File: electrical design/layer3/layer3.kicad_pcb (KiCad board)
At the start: 2 copper layers, 150 x 137.9 mm, 42 parts, among them J1 SH1.0 5P, J10 SH1.0 2P, J11 LAYER1, J12 XH2.54 2P, J2 SH1.0 5P, J3 SH1.0 5P, J4 SH1.0 5P, J5 XH2.54 5P, J6 CAMERA1, J7 CAMERA2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

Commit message: resolve some l2 and l3 board issues
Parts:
- removed R8: 10k, Resistor_SMD:R_0603_1608Metric
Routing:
- net +3V3: track 300.0 -> 295.4 mm
- net /M4CS: track 81.1 -> 84.4 mm
- net /STRAT4: track 48.2 -> 44.9 mm
- net /EN: track 117.9 -> 115.6 mm
- net /STRAT3: track 40.1 -> 39.1 mm
- net +5V: track 363.7 -> 362.8 mm
- net /M3INA: track 60.5 -> 59.8 mm
- net /STRAT2: track 31.0 -> 31.8 mm
- net /M4INA: track 87.8 -> 87.0 mm
- net GNDD: vias 79 -> 126

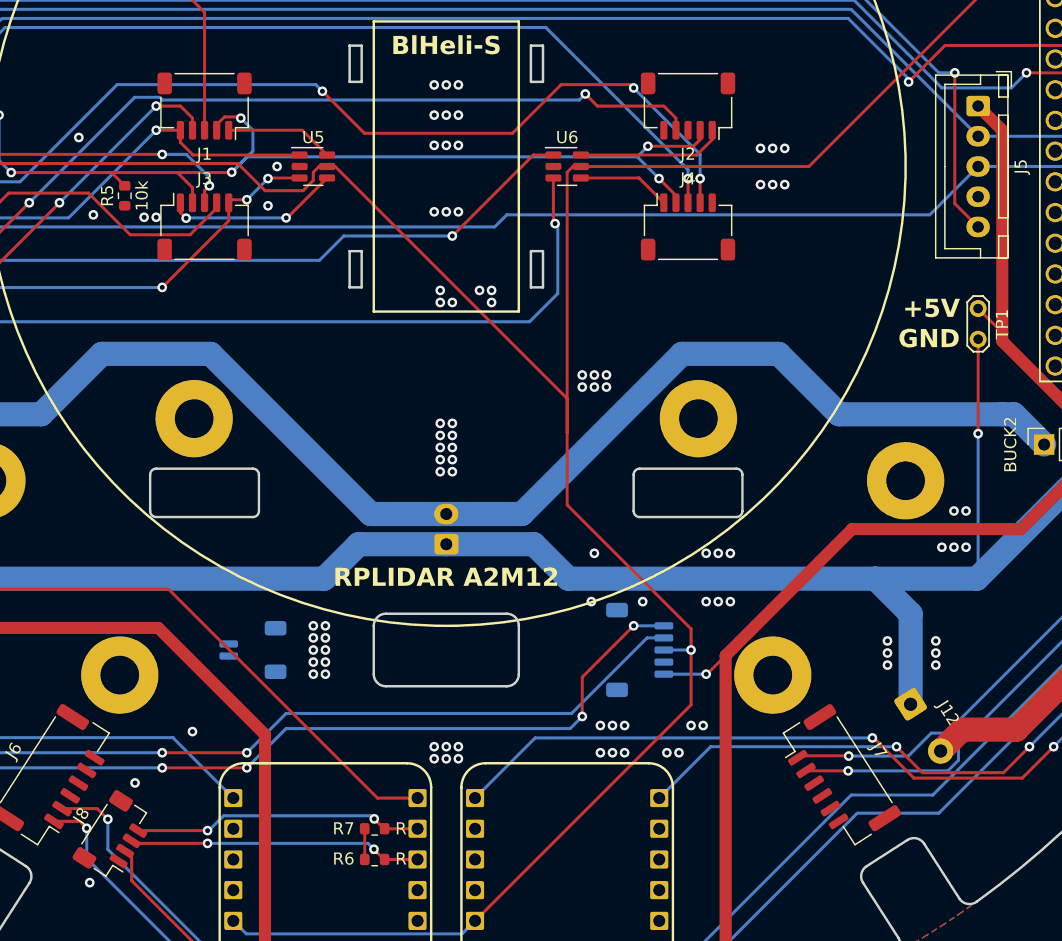
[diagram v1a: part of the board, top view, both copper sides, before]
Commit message: add jlc order number silkscreen
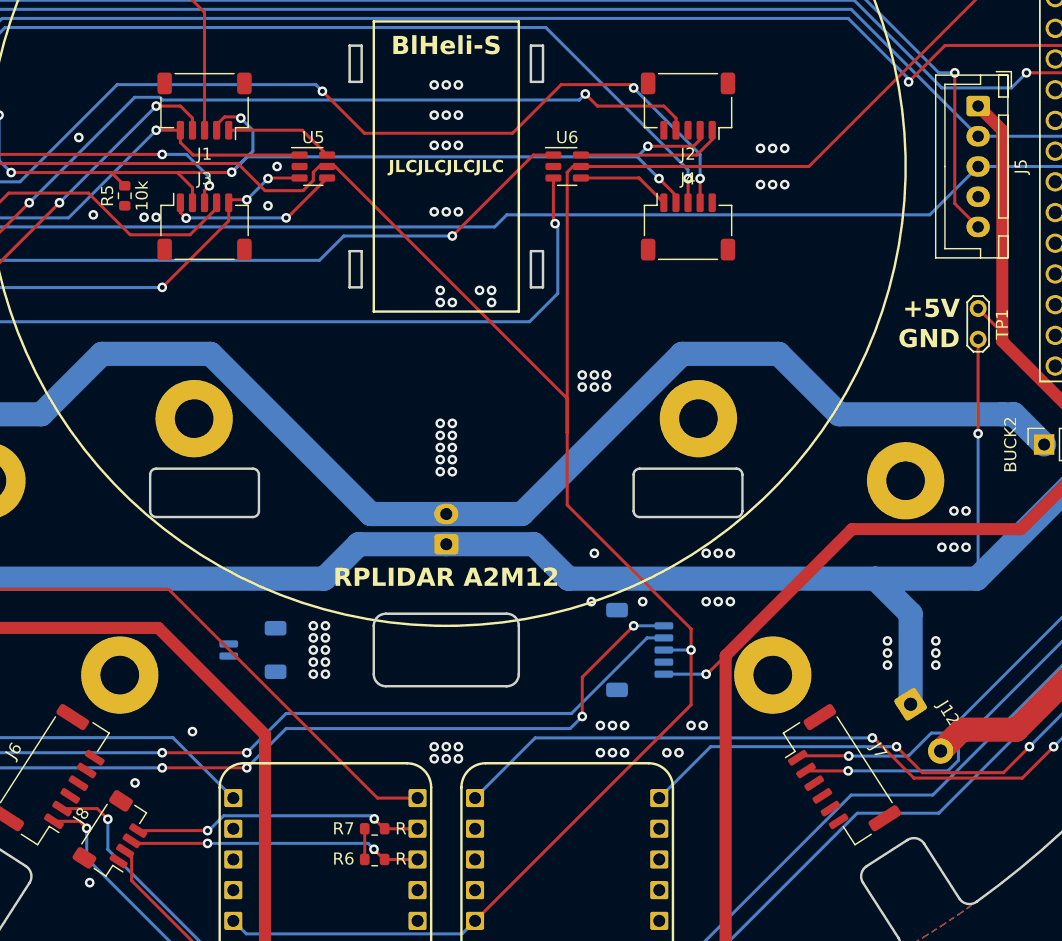
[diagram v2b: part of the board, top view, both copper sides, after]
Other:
- board text added: "JLCJLCJLCJLC"
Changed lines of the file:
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@@
       (plot_on_all_layers_selection 0x0000000_00000000)
       (disableapertmacros false)
-      (usegerberextensions false)
+      (usegerberextensions true)
       (usegerberattributes true)
       (usegerberadvancedattributes true)
-      (creategerberjobfile true)
+      (creategerberjobfile false)
       (dashed_line_dash_ratio 12.000000)
       (dashed_line_gap_ratio 3.000000)
@@
       (plotinvisibletext false)
       (sketchpadsonfab false)
-      (subtractmaskfromsilk false)
+      (subtractmaskfromsilk true)
       (outputformat 1)
       (mirror false)
-      (drillshape 1)
+      (drillshape 0)
       (scaleselection 1)
-      (outputdirectory "")
+      (outputdirectory "fabrication")
     )
   )
@@
     (pad "4" smd roundrect (at 1.5 1.325 57.3) (size 0.6 1.55) (layers "F.Cu" "F.Paste" "F.Mask") (roundrect_rratio 0.25)
       (net 66 "/IMUSCL") (pinfunction "Pin_4") (pintype "passive"))
-    (pad "MP" smd roundrect (at -2.8 -1.2 57.3) (size 1.2 1.8) (layers "F.Cu" "F.Paste" "F.Mask") (roundrect_rratio 0.208333))
-    (pad "MP" smd roundrect (at 2.8 -1.2 57.3) (size 1.2 1.8) (layers "F.Cu" "F.Paste" "F.Mask") (roundrect_rratio 0.208333))
+    (pad "MP" smd roundrect (at -2.8 -1.2 57.3) (size 1.2 1.8) (layers "F.Cu" "F.Paste" "F.Mask") (roundrect_rratio 0.2083333333))
+    (pad "MP" smd roundrect (at 2.8 -1.2 57.3) (size 1.2 1.8) (layers "F.Cu" "F.Paste" "F.Mask") (roundrect_rratio 0.2083333333))
     (model "${KICAD6_3DMODEL_DIR}/Connector_JST.3dshapes/JST_SH_BM04B-SRSS-TB_1x04-1MP_P1.00mm_Vertical.step"
       (offset (xyz 0 1 0))
@@
     (pad "5" smd roundrect (at 2 -2 180) (size 0.6 1.55) (layers "F.Cu" "F.Paste" "F.Mask") (roundrect_rratio 0.25)
       (net 4 "/M1INA") (pinfunction "Pin_5") (pintype "passive"))
-    (pad "MP" smd roundrect (at -3.3 1.875 180) (size 1.2 1.8) (layers "F.Cu" "F.Paste" "F.Mask") (roundrect_rratio 0.208333))
-    (pad "MP" smd roundrect (at 3.3 1.875 180) (size 1.2 1.8) (layers "F.Cu" "F.Paste" "F.Mask") (roundrect_rratio 0.208333))
+    (pad "MP" smd roundrect (at -3.3 1.875 180) (size 1.2 1.8) (layers "F.Cu" "F.Paste" "F.Mask") (roundrect_rratio 0.2083333333))
+    (pad "MP" smd roundrect (at 3.3 1.875 180) (size 1.2 1.8) (layers "F.Cu" "F.Paste" "F.Mask") (roundrect_rratio 0.2083333333))
     (model "${KICAD6_3DMODEL_DIR}/Connector_JST.3dshapes/JST_SH_SM05B-SRSS-TB_1x05-1MP_P1.00mm_Horizontal.step"
       (offset (xyz 0 1 0))
@@
     (pad "5" smd roundrect (at 2 -2) (size 0.6 1.55) (layers "F.Cu" "F.Paste" "F.Mask") (roundrect_rratio 0.25)
       (net 12 "/M3INA") (pinfunction "Pin_5") (pintype "passive"))
-    (pad "MP" smd roundrect (at -3.3 1.875) (size 1.2 1.8) (layers "F.Cu" "F.Paste" "F.Mask") (roundrect_rratio 0.208333))
-    (pad "MP" smd roundrect (at 3.3 1.875) (size 1.2 1.8) (layers "F.Cu" "F.Paste" "F.Mask") (roundrect_rratio 0.208333))
+    (pad "MP" smd roundrect (at -3.3 1.875) (size 1.2 1.8) (layers "F.Cu" "F.Paste" "F.Mask") (roundrect_rratio 0.2083333333))
+    (pad "MP" smd roundrect (at 3.3 1.875) (size 1.2 1.8) (layers "F.Cu" "F.Paste" "F.Mask") (roundrect_rratio 0.2083333333))
     (model "${KICAD6_3DMODEL_DIR}/Connector_JST.3dshapes/JST_SH_SM05B-SRSS-TB_1x05-1MP_P1.00mm_Horizontal.step"
       (offset (xyz 0 1 0))
@@
     (fp_circle (center 4.6 0) (end 5.65 0)
       (stroke (width 0.1) (type solid)) (fill none) (layer "F.Fab"))
-    (pad "1" thru_hole roundrect (at 0 0 302.7) (size 2.1 2.1) (drill 1.1) (layers "*.Cu" "*.Mask") (roundrect_rratio 0.119048)
+    (pad "1" thru_hole roundrect (at 0 0 302.7) (size 2.1 2.1) (drill 1.1) (layers "*.Cu" "*.Mask") (roundrect_rratio 0.1190480952)
       (net 76 "GNDPWR") (pinfunction "Pin_1") (pintype "passive"))
     (pad "2" thru_hole circle (at 4.6 0 302.7) (size 2.1 2.1) (drill 1.1) (layers "*.Cu" "*.Mask")
@@
     (fp_line (start 12.45 3.4) (end 12.45 -2.35)
       (stroke (width 0.1) (type solid)) (layer "F.Fab"))
-    (pad "1" thru_hole roundrect (at 0 0 270) (size 1.7 1.95) (drill 0.95) (layers "*.Cu" "*.Mask") (roundrect_rratio 0.147059)
+    (pad "1" thru_hole roundrect (at 0 0 270) (size 1.7 1.95) (drill 0.95) (layers "*.Cu" "*.Mask") (roundrect_rratio 0.1470588235)
       (net 51 "+5V") (pinfunction "Pin_1") (pintype "passive"))
     (pad "2" thru_hole oval (at 2.5 0 270) (size 1.7 1.95) (drill 0.95) (layers "*.Cu" "*.Mask")
@@
     (pad "5" smd roundrect (at 2 -2) (size 0.6 1.55) (layers "F.Cu" "F.Paste" "F.Mask") (roundrect_rratio 0.25)
       (net 16 "/M4INA") (pinfunction "Pin_5") (pintype "passive"))
-    (pad "MP" smd roundrect (at -3.3 1.875) (size 1.2 1.8) (layers "F.Cu" "F.Paste" "F.Mask") (roundrect_rratio 0.208333))
-    (pad "MP" smd roundrect (at 3.3 1.875) (size 1.2 1.8) (layers "F.Cu" "F.Paste" "F.Mask") (roundrect_rratio 0.208333))
+    (pad "MP" smd roundrect (at -3.3 1.875) (size 1.2 1.8) (layers "F.Cu" "F.Paste" "F.Mask") (roundrect_rratio 0.2083333333))
+    (pad "MP" smd roundrect (at 3.3 1.875) (size 1.2 1.8) (layers "F.Cu" "F.Paste" "F.Mask") (roundrect_rratio 0.2083333333))
     (model "${KICAD6_3DMODEL_DIR}/Connector_JST.3dshapes/JST_SH_SM05B-SRSS-TB_1x05-1MP_P1.00mm_Horizontal.step"
       (offset (xyz 0 1 0))
@@
     (pad "5" smd roundrect (at 2 -2 180) (size 0.6 1.55) (layers "F.Cu" "F.Paste" "F.Mask") (roundrect_rratio 0.25)
       (net 8 "/M2INA") (pinfunction "Pin_5") (pintype "passive"))
-    (pad "MP" smd roundrect (at -3.3 1.875 180) (size 1.2 1.8) (layers "F.Cu" "F.Paste" "F.Mask") (roundrect_rratio 0.208333))
-    (pad "MP" smd roundrect (at 3.3 1.875 180) (size 1.2 1.8) (layers "F.Cu" "F.Paste" "F.Mask") (roundrect_rratio 0.208333))
+    (pad "MP" smd roundrect (at -3.3 1.875 180) (size 1.2 1.8) (layers "F.Cu" "F.Paste" "F.Mask") (roundrect_rratio 0.2083333333))
+    (pad "MP" smd roundrect (at 3.3 1.875 180) (size 1.2 1.8) (layers "F.Cu" "F.Paste" "F.Mask") (roundrect_rratio 0.2083333333))
     (model "${KICAD6_3DMODEL_DIR}/Connector_JST.3dshapes/JST_SH_SM05B-SRSS-TB_1x05-1MP_P1.00mm_Horizontal.step"
       (offset (xyz 0 1 0))
@@
     (pad "5" smd roundrect (at 2 2 90) (size 0.6 1.55) (layers "B.Cu" "B.Paste" "B.Mask") (roundrect_rratio 0.25)
       (net 69 "/L1TX") (pinfunction "Pin_5") (pintype "passive"))
-    (pad "MP" smd roundrect (at -3.3 -1.875 90) (size 1.2 1.8) (layers "B.Cu" "B.Paste" "B.Mask") (roundrect_rratio 0.208333))
-    (pad "MP" smd roundrect (at 3.3 -1.875 90) (size 1.2 1.8) (layers "B.Cu" "B.Paste" "B.Mask") (roundrect_rratio 0.208333))
+    (pad "MP" smd roundrect (at -3.3 -1.875 90) (size 1.2 1.8) (layers "B.Cu" "B.Paste" "B.Mask") (roundrect_rratio 0.2083333333))
+    (pad "MP" smd roundrect (at 3.3 -1.875 90) (size 1.2 1.8) (layers "B.Cu" "B.Paste" "B.Mask") (roundrect_rratio 0.2083333333))
     (model "${KICAD6_3DMODEL_DIR}/Connector_JST.3dshapes/JST_SH_SM05B-SRSS-TB_1x05-1MP_P1.00mm_Horizontal.step"
       (offset (xyz 0 1 0))
@@
     (pad "2" smd roundrect (at 0.5 2 270) (size 0.6 1.55) (layers "B.Cu" "B.Paste" "B.Mask") (roundrect_rratio 0.25)
       (net 75 "GNDD") (pinfunction "Pin_2") (pintype "passive"))
-    (pad "MP" smd roundrect (at -1.8 -1.875 270) (size 1.2 1.8) (layers "B.Cu" "B.Paste" "B.Mask") (roundrect_rratio 0.208333))
-    (pad "MP" smd roundrect (at 1.8 -1.875 270) (size 1.2 1.8) (layers "B.Cu" "B.Paste" "B.Mask") (roundrect_rratio 0.208333))
+    (pad "MP" smd roundrect (at -1.8 -1.875 270) (size 1.2 1.8) (layers "B.Cu" "B.Paste" "B.Mask") (roundrect_rratio 0.2083333333))
+    (pad "MP" smd roundrect (at 1.8 -1.875 270) (size 1.2 1.8) (layers "B.Cu" "B.Paste" "B.Mask") (roundrect_rratio 0.2083333333))
     (model "${KICAD6_3DMODEL_DIR}/Connector_JST.3dshapes/JST_SH_SM02B-SRSS-TB_1x02-1MP_P1.00mm_Horizontal.step"
       (offset (xyz 0 1 0))
@@
     (fp_line (start 4.95 2.35) (end -2.45 2.35)
       (stroke (width 0.1) (type solid)) (layer "B.Fab"))
-    (pad "1" thru_hole roundrect (at 0 0 90) (size 1.7 2) (drill 1) (layers "*.Cu" "*.Mask") (roundrect_rratio 0.147059)
+    (pad "1" thru_hole roundrect (at 0 0 90) (size 1.7 2) (drill 1) (layers "*.Cu" "*.Mask") (roundrect_rratio 0.1470588235)
       (net 76 "GNDPWR") (pinfunction "Pin_1") (pintype "passive"))
     (pad "2" thru_hole oval (at 2.5 0 90) (size 1.7 2) (drill 1) (layers "*.Cu" "*.Mask")
@@
     (effects (font (size 1.5 1.5) (thickness 0.3) bold) (justify right))
   )
+  (gr_text "JLCJLCJLCJLC" (at 105 105) (layer "F.SilkS")
+    (effects (font (size 1 1) (thickness 0.2) bold))
+  )
   (gr_text "ON" (at 50 67.75) (layer "F.SilkS")

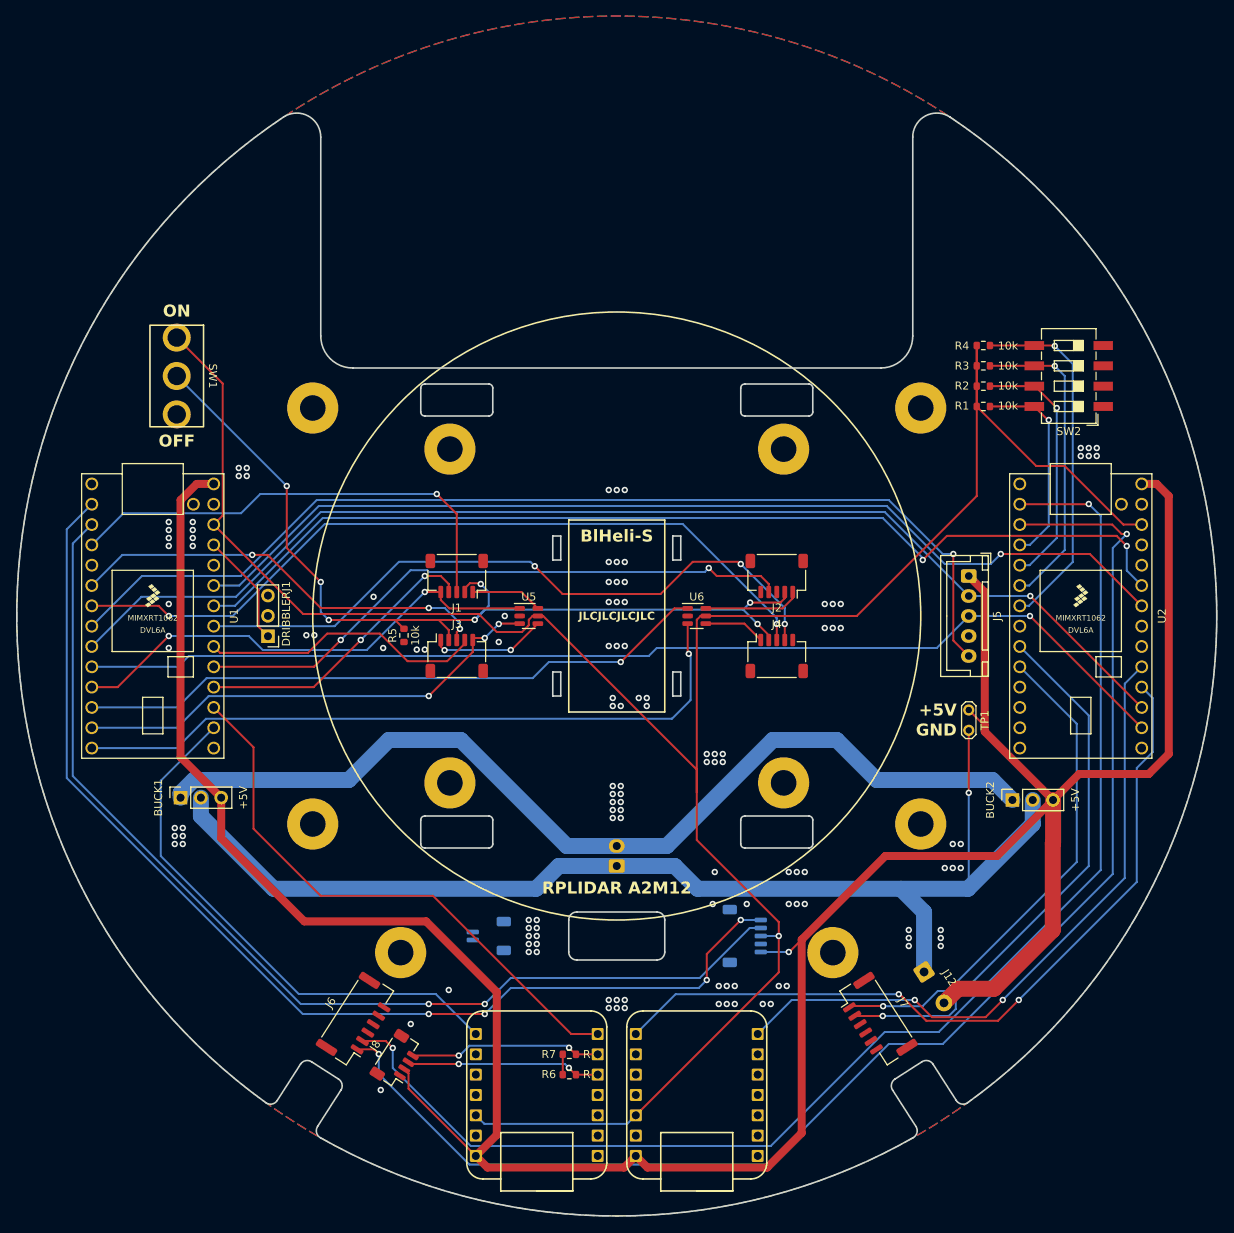
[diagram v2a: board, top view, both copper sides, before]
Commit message: reroute 90 deg traces on l3 pcb
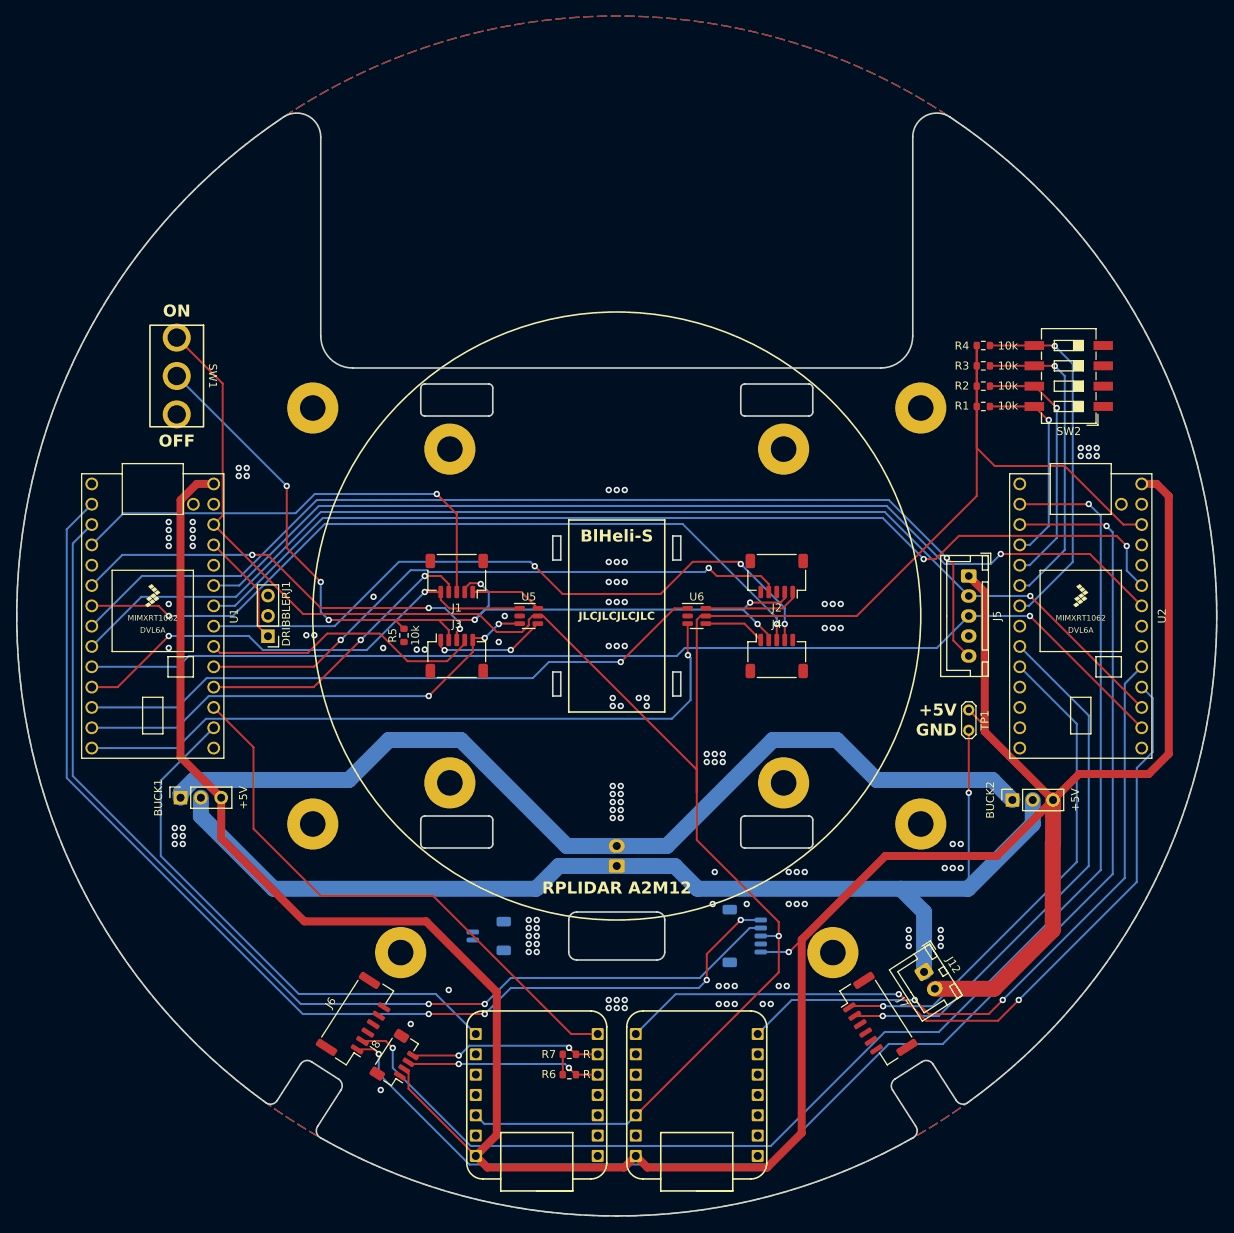
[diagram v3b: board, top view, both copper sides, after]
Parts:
- J12: footprint Connector_Wire:SolderWire-0.5sqmm_1x02_P4.6mm_D0.9mm_OD2.1mm -> Connector_JST:JST_XH_B2B-XH-A_1x02_P2.50mm_Vertical
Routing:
- net +3V3: track 295.4 -> 298.5 mm
- net /CAM1RX: track 174.0 -> 171.7 mm
- net /LIDARPWM: track 130.6 -> 129.8 mm
- net /CAM2TX: track 68.8 -> 68.0 mm
